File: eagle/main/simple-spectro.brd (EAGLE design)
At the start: 99.1 x 73.7 mm, 52 parts, among them CON1 BAT, CON2 SPI, CON3 SPI, CON4 VIBR, IC1 32U4, IC2 MCP73831T, IC3 MCP1703CB, IC4 DMP1045U or DMG2302, Q6 BSP75, U1 NCT75DMR2G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

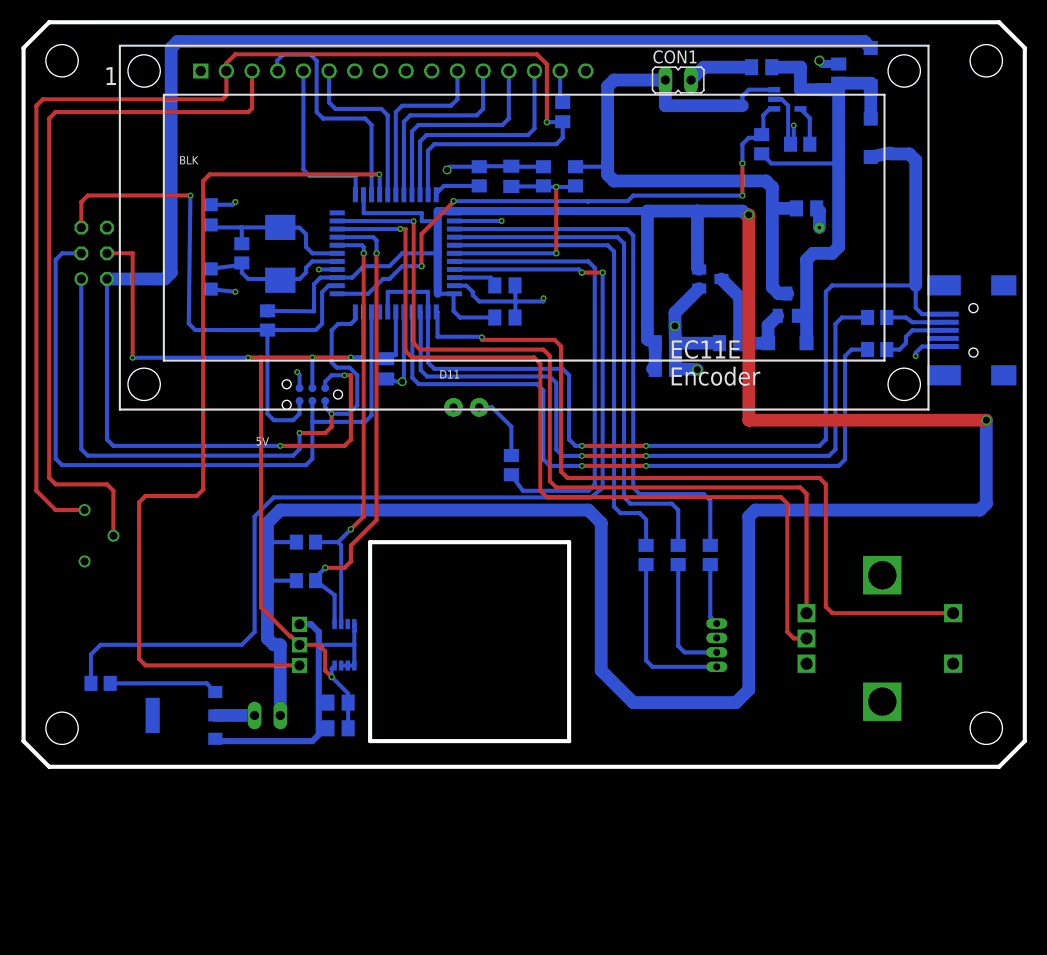
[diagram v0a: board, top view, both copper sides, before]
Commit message: add resistor to LCD and move power to PE2
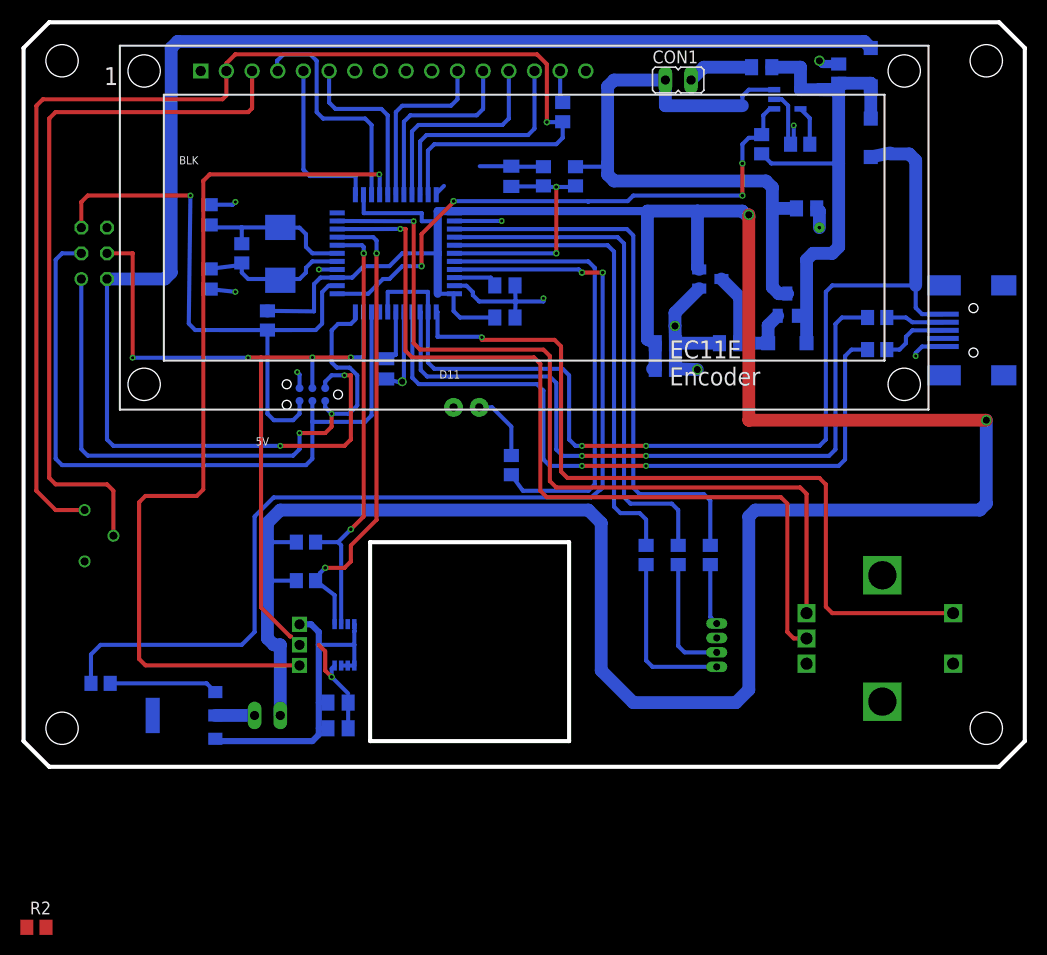
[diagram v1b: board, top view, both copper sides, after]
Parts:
- removed R13: 10k, rcl:R0805
- added R2: 100, rcl:R0805
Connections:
- new net N$4: POT.1, R2.1
- net GND: now also R2.2; no longer POT.1, R13.1
- net HWB: now also C12.1, C13.2, U$7.VDD, U1.8; no longer R13.2
- net MOSI: no longer C12.1, C13.2, U$7.VDD, U1.8
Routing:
- net MOSI: track 85.9 -> 72.2 mm, vias 5 -> 4
- net HWB: track 4.68 -> 11.0 mm, vias 0 -> 1
- net GND: track 133.7 -> 130.4 mm, vias 14 -> 13
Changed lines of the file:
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@@
 <?xml version="1.0" encoding="utf-8"?>
 <!DOCTYPE eagle SYSTEM "eagle.dtd">
-<eagle version="8.5.0">
+<eagle version="8.4.0">
 <drawing>
 <settings>
@@
 <param name="dpMaxLengthDifference" value="10mm"/>
 <param name="dpGapFactor" value="2.5"/>
-<param name="checkAngle" value="0"/>
 <param name="checkFont" value="1"/>
 <param name="checkRestrict" value="0"/>
 <param name="checkStop" value="0"/>
-<param name="checkValues" value="0"/>
 <param name="useDiameter" value="13"/>
 <param name="maxErrors" value="50"/>
@@
 <attribute name="VALUE" x="17.1785875" y="57.04928125" size="1.27" layer="28" rot="MR270"/>
 </element>
-<element name="R13" library="rcl" library_urn="urn:adsk.eagle:library:334" package="R0805" package3d_urn="urn:adsk.eagle:package:23553/2" value="10k" x="45.085" y="58.42" smashed="yes" rot="MR270">
-<attribute name="ELECROW" value="C17414" x="45.085" y="58.42" size="1.778" layer="28" rot="MR270" display="off"/>
-<attribute name="LCSC" value="C17414" x="45.085" y="58.42" size="1.778" layer="28" rot="MR270" display="off"/>
-<attribute name="NAME" x="43.815" y="59.055" size="1.27" layer="26" rot="MR270"/>
-<attribute name="VALUE" x="44.02455" y="60.0837" size="1.27" layer="28" rot="MR270"/>
-</element>
 <element name="C9" library="rcl" library_urn="urn:adsk.eagle:library:334" package="C0805K" package3d_urn="urn:adsk.eagle:package:23681/2" value="100nF" x="35.8775" y="39.37" smashed="yes" rot="MR90">
 <attribute name="ELECROW" value="C49678" x="35.8775" y="39.37" size="1.778" layer="28" rot="MR90" display="off"/>
@@
 <attribute name="LCSC" value="C144342" x="67.945" y="48.26" size="1.778" layer="28" rot="MR90" display="off"/>
 </element>
+<element name="R2" library="rcl" package="R0805" value="100" x="1.27" y="-15.875">
+<attribute name="ELECROW" value="C17408" x="1.27" y="-15.875" size="1.778" layer="27" display="off"/>
+<attribute name="LCSC" value="C17408" x="1.27" y="-15.875" size="1.778" layer="27" display="off"/>
+</element>
 </elements>
 <signals>
@@
 <contactref element="IC1" pad="15"/>
 <contactref element="IC1" pad="5"/>
-<contactref element="R13" pad="1"/>
 <contactref element="IC1" pad="35"/>
 <contactref element="IC1" pad="43"/>
@@
 <via x="27.0764" y="39.0398" extent="1-16" drill="0.3048" shape="square"/>
 <contactref element="LED5" pad="GND"/>
-<via x="41.91" y="59.055" extent="1-16" drill="0.6" shape="square"/>
 <wire x1="37.63" y1="37.97" x2="37.465" y2="37.97" width="0.4064" layer="16"/>
 <wire x1="37.465" y1="37.97" x2="37.465" y2="38.1" width="0.4064" layer="16"/>
 <via x="37.465" y="38.1" extent="1-16" drill="0.6" shape="square"/>
-<contactref element="POT" pad="1"/>
 <contactref element="CON1" pad="2"/>
 <wire x1="18.415" y1="47.26" x2="20.955" y2="46.99" width="0.4064" layer="16"/>
@@
 <wire x1="48.31" y1="59.37" x2="48.26" y2="59.42" width="0.4064" layer="16"/>
 <wire x1="48.26" y1="59.42" x2="45.135" y2="59.42" width="0.4064" layer="16"/>
-<wire x1="45.135" y1="59.42" x2="45.085" y2="59.37" width="0.4064" layer="16"/>
-<wire x1="45.085" y1="59.37" x2="42.225" y2="59.37" width="0.4064" layer="16"/>
-<wire x1="42.225" y1="59.37" x2="41.91" y2="59.055" width="0.4064" layer="16"/>
 <contactref element="C13" pad="1"/>
 <contactref element="C12" pad="2"/>
@@
 <wire x1="78.74" y1="69.85" x2="79.06" y2="69.53" width="0.8128" layer="16"/>
 <wire x1="79.06" y1="69.53" x2="80.645" y2="69.53" width="0.8128" layer="16"/>
+<contactref element="R2" pad="2"/>
+<wire x1="75.01214375" y1="66.04" x2="78.74" y2="69.85" width="0" layer="19" extent="16-16"/>
+<wire x1="72.025" y1="69.215" x2="74.2649" y2="66.04" width="0" layer="19" extent="16-16"/>
+<wire x1="78.47" y1="55.245" x2="76.2" y2="61.595" width="0" layer="19" extent="16-16"/>
+<wire x1="55.63" y1="68.84" x2="66.04" y2="67.945" width="0" layer="19" extent="1-1"/>
+<wire x1="51.435" y1="59.37" x2="55.63" y2="68.84" width="0" layer="19" extent="16-16"/>
+<wire x1="47.305" y1="54" x2="48.31" y2="59.37" width="0" layer="19" extent="16-16"/>
+<wire x1="42.63" y1="47.6" x2="42.63" y2="54" width="0" layer="19" extent="16-16"/>
+<wire x1="37.63" y1="45" x2="42.63" y2="47.6" width="0" layer="19" extent="16-16"/>
+<wire x1="42.545" y1="35.56" x2="37.63" y2="37.97" width="0" layer="19" extent="16-16"/>
+<wire x1="31.03" y1="49.2" x2="37.63" y2="45" width="0" layer="19" extent="16-16"/>
+<wire x1="32.83" y1="56.6" x2="31.03" y2="49.2" width="0" layer="19" extent="16-16"/>
+<wire x1="20.955" y1="55.88" x2="27.69" y2="59.0804" width="0" layer="19" extent="16-16"/>
+<wire x1="18.415" y1="47.26" x2="18.415" y2="55.61" width="0" layer="19" extent="16-16"/>
+<wire x1="27.305" y1="38.8112" x2="35.8775" y2="38.37" width="0" layer="19" extent="16-16"/>
+<wire x1="17.53" y1="68.84" x2="27.69" y2="68.84" width="0" layer="19" extent="1-1"/>
+<wire x1="8.255" y1="53.34" x2="18.415" y2="55.61" width="0" layer="19" extent="16-16"/>
+<wire x1="64.45" y1="44.915" x2="51.435" y2="46.0375" width="0" layer="19" extent="16-16"/>
+<wire x1="88.9" y1="41.58" x2="78.74" y2="53.34" width="0" layer="19" extent="16-16"/>
+<wire x1="27.305" y1="14.097" x2="27.305" y2="37.465" width="0" layer="19" extent="16-16"/>
+<wire x1="2.22" y1="-15.875" x2="19.203" y2="2.54" width="0" layer="19" extent="1-16"/>
+<wire x1="68.58" y1="12.7475" x2="66.65595" y2="39.30015" width="0" layer="19" extent="1-1"/>
+<wire x1="77.47" y1="10.2" x2="68.58" y2="12.7475" width="0" layer="19" extent="1-1"/>
+<wire x1="91.97" y1="10.2" x2="77.47" y2="10.2" width="0" layer="19" extent="1-1"/>
 </signal>
 <signal name="SCK">
@@
 <wire x1="33.63" y1="45" x2="33.63" y2="40.5253" width="0.4064" layer="16"/>
 <wire x1="33.63" y1="40.5253" x2="32.385" y2="40.5003" width="0.4064" layer="16"/>
-<contactref element="U$7" pad="VDD"/>
-<contactref element="C12" pad="1"/>
-<contactref element="C13" pad="2"/>
-<contactref element="U1" pad="8"/>
-<wire x1="29.21" y1="12.065" x2="29.845" y2="11.43" width="0.4064" layer="1"/>
-<wire x1="29.845" y1="11.43" x2="29.845" y2="9.525" width="0.4064" layer="1"/>
-<wire x1="29.845" y1="9.525" x2="30.48" y2="8.89" width="0.4064" layer="1"/>
-<via x="30.48" y="8.89" extent="1-16" drill="0.35"/>
-<wire x1="30.48" y1="8.89" x2="30.48" y2="9.72" width="0.4064" layer="16"/>
-<wire x1="30.775" y1="10.015" x2="30.48" y2="9.72" width="0.4064" layer="16"/>
-<wire x1="29.21" y1="12.065" x2="27.305" y2="12.065" width="0.4064" layer="1"/>
-<wire x1="32.115" y1="6.35" x2="32.115" y2="7.255" width="0.4064" layer="16"/>
-<wire x1="32.115" y1="7.255" x2="30.48" y2="8.89" width="0.4064" layer="16"/>
-<wire x1="32.115" y1="3.81" x2="32.115" y2="6.35" width="0.4064" layer="16"/>
-<wire x1="27.305" y1="12.065" x2="26.4762" y2="12.8938" width="0.4064" layer="1"/>
 <wire x1="26.4762" y1="12.8938" x2="26.36728125" y2="12.8938" width="0.4064" layer="1"/>
 <wire x1="26.36728125" y1="12.8938" x2="23.495" y2="15.76608125" width="0.4064" layer="1"/>
@@
 <signal name="HWB">
 <contactref element="IC1" pad="33"/>
-<contactref element="R13" pad="2"/>
 <wire x1="40.83" y1="56.6" x2="40.83" y2="56.705" width="0.4064" layer="16"/>
-<wire x1="41.595" y1="57.47" x2="45.085" y2="57.47" width="0.4064" layer="16"/>
 <wire x1="40.83" y1="56.705" x2="41.595" y2="57.47" width="0.4064" layer="16"/>
+<contactref element="U$7" pad="VDD"/>
+<contactref element="C12" pad="1"/>
+<contactref element="C13" pad="2"/>
+<wire x1="32.115" y1="3.81" x2="32.115" y2="6.35" width="0.4064" layer="16"/>
+<contactref element="U1" pad="8"/>
+<wire x1="29.21" y1="12.065" x2="29.845" y2="11.43" width="0.4064" layer="1"/>
+<wire x1="29.845" y1="11.43" x2="29.845" y2="9.525" width="0.4064" layer="1"/>
+<wire x1="29.845" y1="9.525" x2="30.48" y2="8.89" width="0.4064" layer="1"/>
+<via x="30.48" y="8.89" extent="1-16" drill="0.35"/>
+<wire x1="30.48" y1="8.89" x2="30.48" y2="9.72" width="0.4064" layer="16"/>
+<wire x1="30.775" y1="10.015" x2="30.48" y2="9.72" width="0.4064" layer="16"/>
+<wire x1="32.115" y1="7.255" x2="30.48" y2="8.89" width="0.4064" layer="16"/>
+<wire x1="29.21" y1="12.065" x2="40.83" y2="56.6" width="0" layer="19" extent="1-16"/>
+<wire x1="32.115" y1="6.35" x2="32.115" y2="7.255" width="0" layer="19" extent="16-16"/>
+<wire x1="27.305" y1="12.065" x2="29.21" y2="12.065" width="0" layer="19" extent="1-1"/>
 </signal>
 <signal name="N$42">
@@
 <wire x1="36.83" y1="64.77" x2="36.83" y2="56.6" width="0.4064" layer="16"/>
 </signal>
+<signal name="N$4">
+<contactref element="POT" pad="1"/>
+<contactref element="R2" pad="1"/>
+<wire x1="0.32" y1="-15.875" x2="6.04" y2="20.32" width="0" layer="19" extent="1-1"/>
+</signal>
 </signals>

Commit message: power the NCT75 directly because sleep mode is under 12uA
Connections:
- net HWB: no longer U1.8
- net VCC: now also U1.8
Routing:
- net HWB: track 11.0 -> 3.73 mm, vias 1 -> 0
- net VCC: track 294.2 -> 301.4 mm, vias 2 -> 3
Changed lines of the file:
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@@
 <contactref element="C13" pad="2"/>
 <wire x1="32.115" y1="3.81" x2="32.115" y2="6.35" width="0.4064" layer="16"/>
-<contactref element="U1" pad="8"/>
-<wire x1="29.21" y1="12.065" x2="29.845" y2="11.43" width="0.4064" layer="1"/>
-<wire x1="29.845" y1="11.43" x2="29.845" y2="9.525" width="0.4064" layer="1"/>
-<wire x1="29.845" y1="9.525" x2="30.48" y2="8.89" width="0.4064" layer="1"/>
-<via x="30.48" y="8.89" extent="1-16" drill="0.35"/>
-<wire x1="30.48" y1="8.89" x2="30.48" y2="9.72" width="0.4064" layer="16"/>
-<wire x1="30.775" y1="10.015" x2="30.48" y2="9.72" width="0.4064" layer="16"/>
-<wire x1="32.115" y1="7.255" x2="30.48" y2="8.89" width="0.4064" layer="16"/>
-<wire x1="29.21" y1="12.065" x2="40.83" y2="56.6" width="0" layer="19" extent="1-16"/>
-<wire x1="32.115" y1="6.35" x2="32.115" y2="7.255" width="0" layer="19" extent="16-16"/>
-<wire x1="27.305" y1="12.065" x2="29.21" y2="12.065" width="0" layer="19" extent="1-1"/>
+<wire x1="27.305" y1="12.065" x2="40.83" y2="56.6" width="0" layer="19" extent="16-16"/>
+<wire x1="32.115" y1="6.35" x2="27.305" y2="12.065" width="0" layer="19" extent="16-16"/>
 </signal>
 <signal name="N$42">
@@
 <wire x1="36.195" y1="49.53" x2="37.465" y2="50.8" width="0.4064" layer="16"/>
 <wire x1="37.465" y1="50.8" x2="40.97655" y2="50.8" width="0.4064" layer="16"/>
+<contactref element="U1" pad="8"/>
+<wire x1="29.21" y1="12.065" x2="29.845" y2="11.43" width="0.4064" layer="1"/>
+<wire x1="29.845" y1="11.43" x2="29.845" y2="9.525" width="0.4064" layer="1"/>
+<wire x1="29.845" y1="9.525" x2="30.48" y2="8.89" width="0.4064" layer="1"/>
+<via x="30.48" y="8.89" extent="1-16" drill="0.35"/>
+<wire x1="30.48" y1="8.89" x2="30.48" y2="9.72" width="0.4064" layer="16"/>
+<wire x1="30.775" y1="10.015" x2="30.48" y2="9.72" width="0.4064" layer="16"/>
+<wire x1="32.115" y1="7.255" x2="30.48" y2="8.89" width="0.4064" layer="16"/>
+<wire x1="25.4" y1="12.065" x2="29.21" y2="12.065" width="0" layer="19" extent="1-16"/>
 </signal>
 <signal name="N$15">

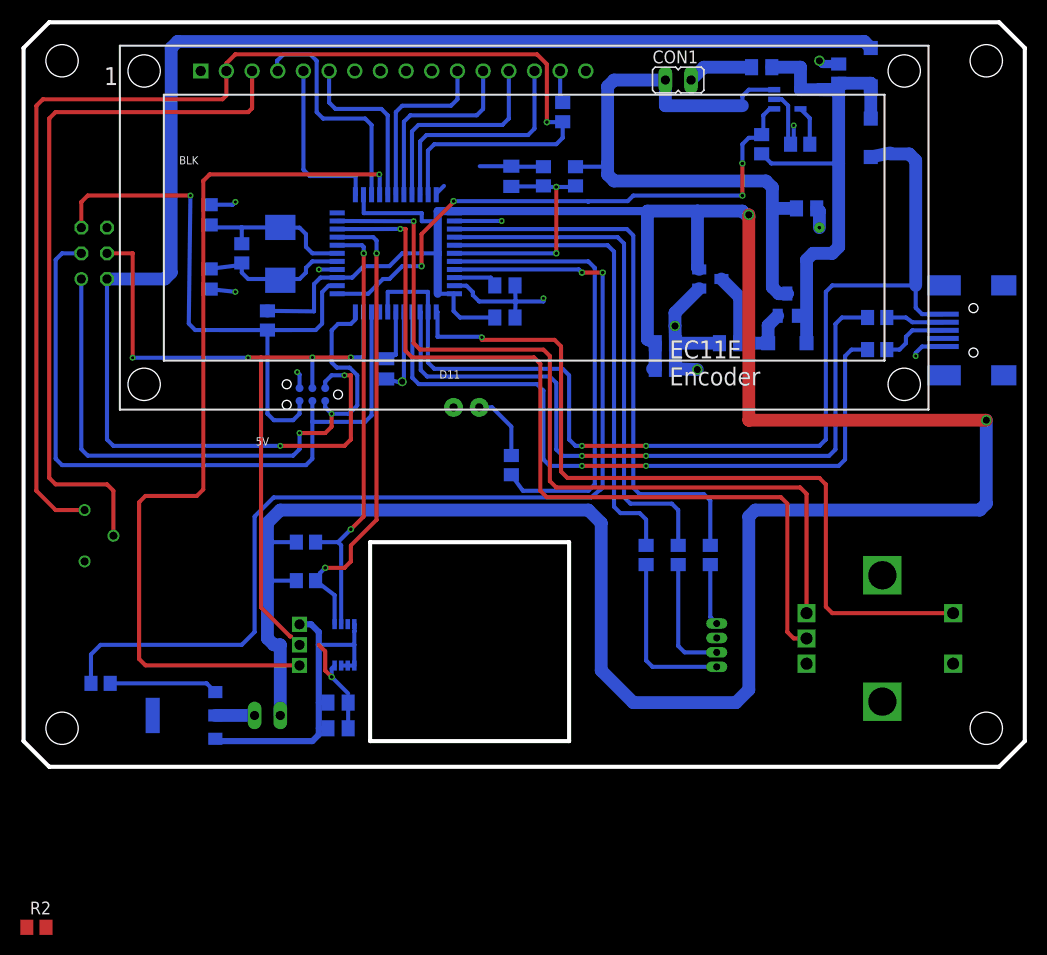
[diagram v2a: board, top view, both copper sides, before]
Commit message: add resistor to LCD in serial, switch D11 and A5, use HSB for power of TSL237, add 2 resistors for battery status with A5
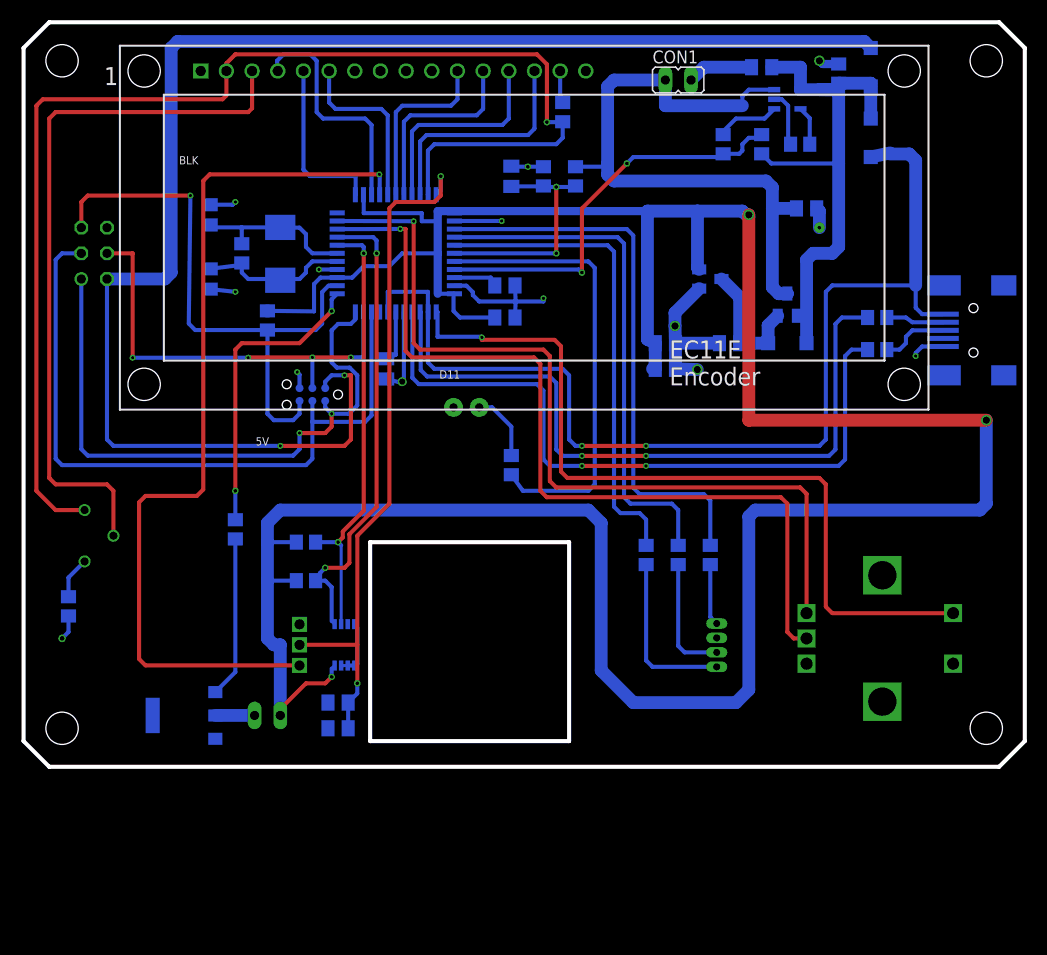
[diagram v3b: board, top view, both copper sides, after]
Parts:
- added R13: 10k, rcl:R0805
- IC4: value DMP1045U or DMG2302 -> DMP1045U
- moved R2 31.9 mm to (4.45, 15.9), flipped to the bottom, turned to 270 degrees
- moved R20 20.3 mm to (21.0, 23.5), turned to 270 degrees
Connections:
- new net N$5: IC2.1, R13.2
- net A5: now also R1.2, R13.1; no longer R20.1
- net D11: now also R20.1; no longer IC2.1, R1.2
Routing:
- net HWB: track 3.73 -> 68.5 mm, vias 0 -> 2
- net A5: track 103.4 -> 40.5 mm
- net GND: track 130.4 -> 99.9 mm, vias 13 -> 14
- net MOSI: track 72.2 -> 43.2 mm
- net D11: track 56.8 -> 29.9 mm, vias 4 -> 2
- net N$5: track 0.00 -> 6.29 mm
- net N$8: track 10.8 -> 16.0 mm
- net N$4: track 0.00 -> 4.16 mm
- net VCC: track 301.4 -> 302.4 mm
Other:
- board text added: "Simple spectro V 1.6.0"
- board text added: "Simple spectro V1.6.0"
- board text removed: "Simple spectro V 1.5.0"
- board text removed: "Simple spectro V1.5.0"
